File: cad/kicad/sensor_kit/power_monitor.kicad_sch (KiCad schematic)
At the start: 20 parts, among them U2 INA3221

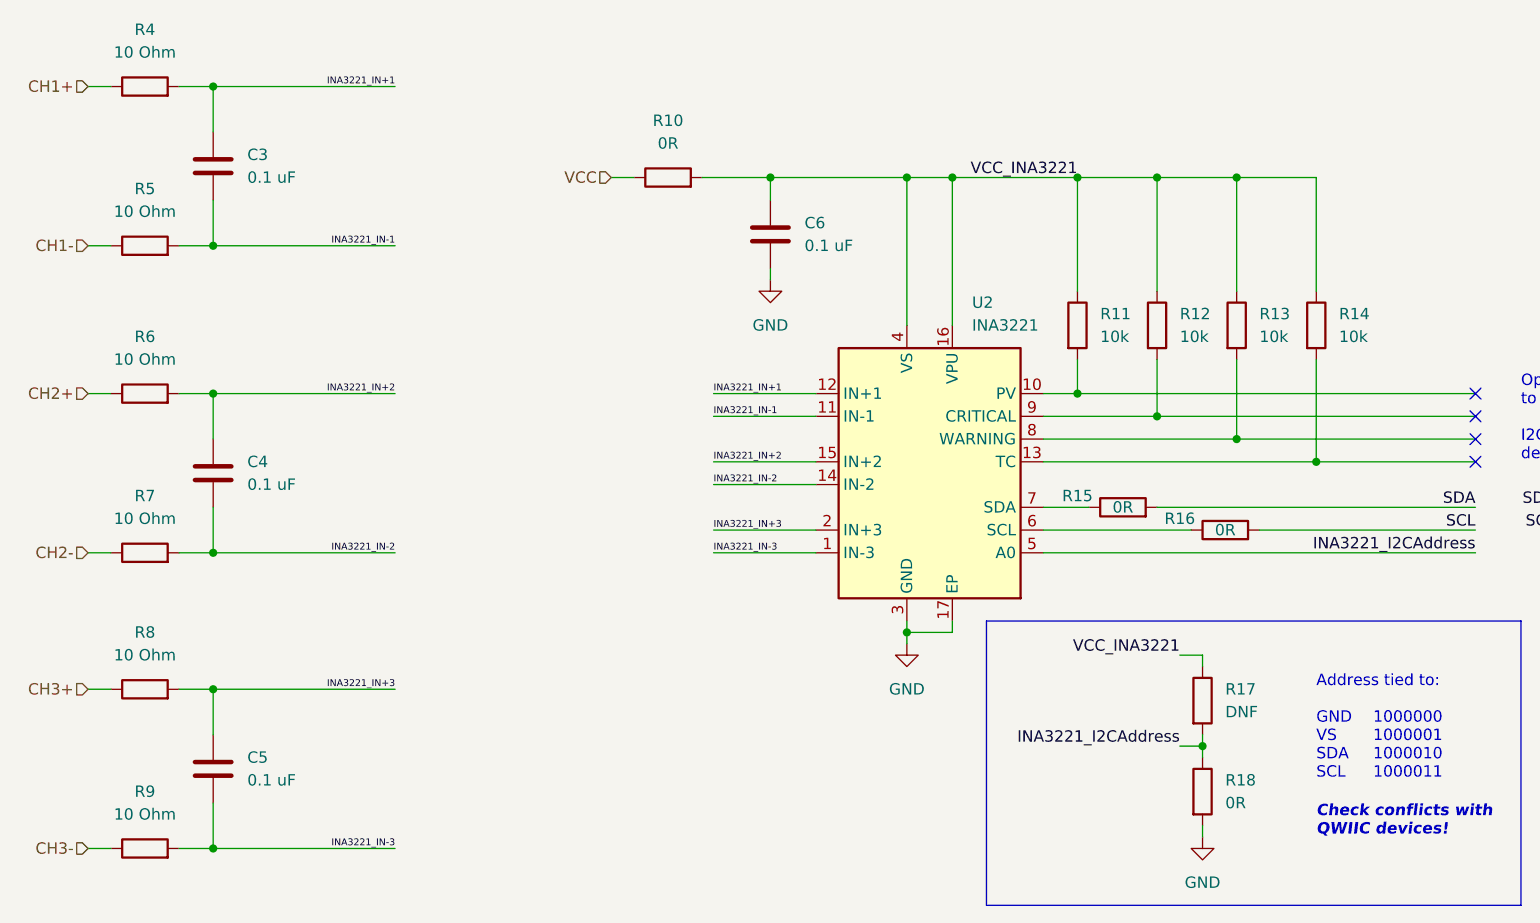
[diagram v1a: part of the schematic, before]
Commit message: adds further sensors to board layout
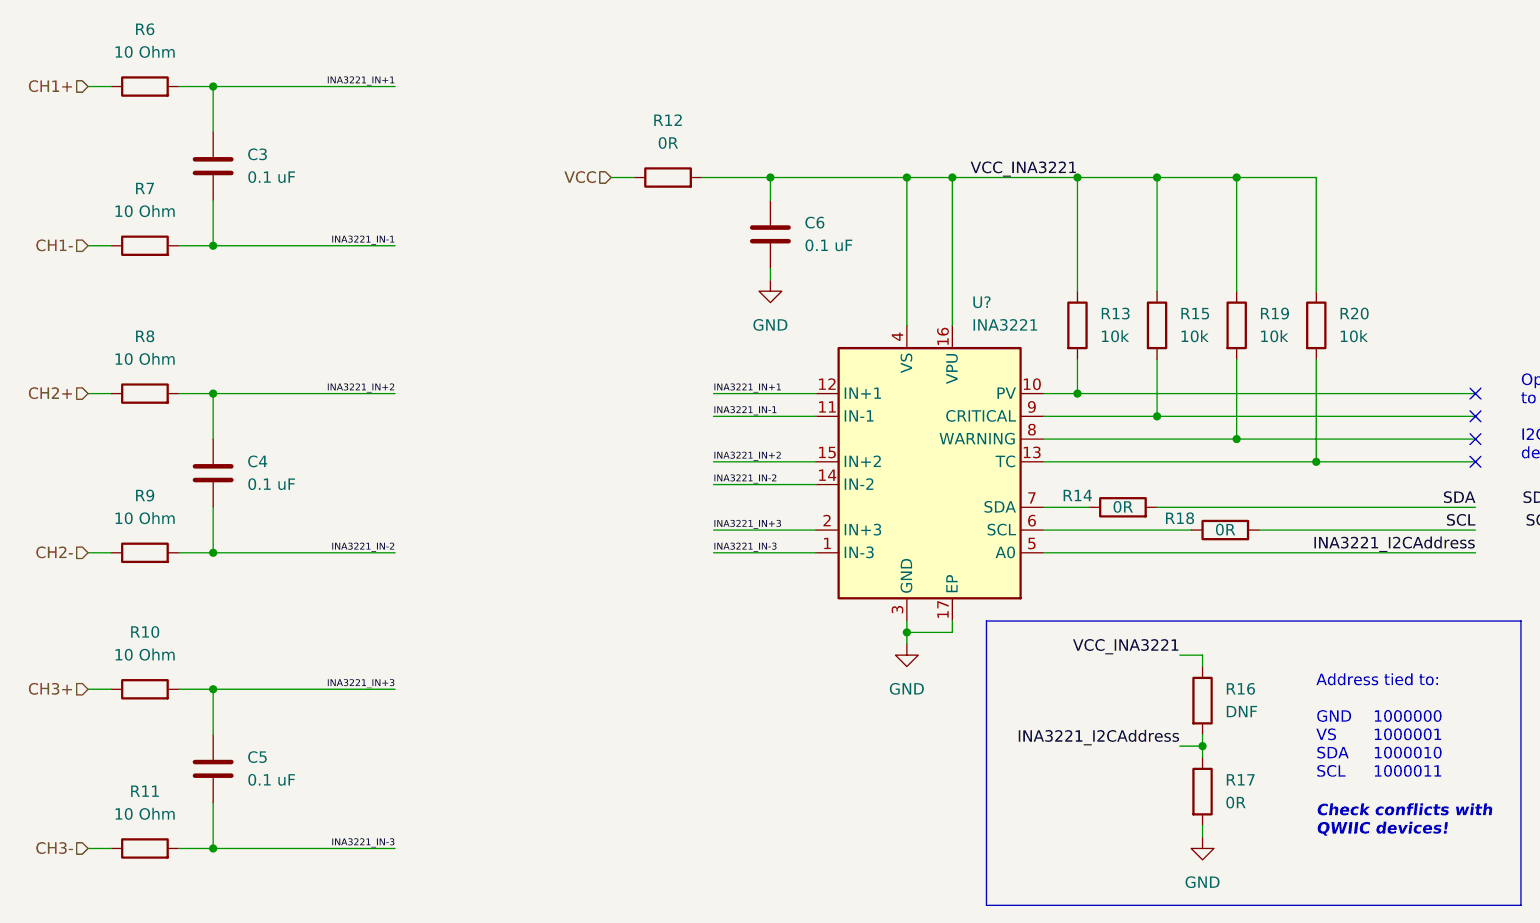
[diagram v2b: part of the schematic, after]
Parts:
- R10: renamed from R8; footprint (none) -> Resistor_SMD:R_1206_3216Metric_Pad1.30x1.75mm_HandSolder
- R11: renamed from R9; footprint (none) -> Resistor_SMD:R_1206_3216Metric_Pad1.30x1.75mm_HandSolder
- R12: renamed from R10; footprint (none) -> Resistor_SMD:R_0805_2012Metric_Pad1.20x1.40mm_HandSolder
- R13: renamed from R11; footprint (none) -> Resistor_SMD:R_0805_2012Metric_Pad1.20x1.40mm_HandSolder
- R14: renamed from R15; footprint (none) -> Resistor_SMD:R_0805_2012Metric_Pad1.20x1.40mm_HandSolder
- R15: renamed from R12; footprint (none) -> Resistor_SMD:R_0805_2012Metric_Pad1.20x1.40mm_HandSolder
- R16: renamed from R17; footprint (none) -> Resistor_SMD:R_0805_2012Metric_Pad1.20x1.40mm_HandSolder
- R17: renamed from R18; footprint (none) -> Resistor_SMD:R_0805_2012Metric_Pad1.20x1.40mm_HandSolder
- R18: renamed from R16; footprint (none) -> Resistor_SMD:R_0805_2012Metric_Pad1.20x1.40mm_HandSolder
- R19: renamed from R13; footprint (none) -> Resistor_SMD:R_0805_2012Metric_Pad1.20x1.40mm_HandSolder
- R20: renamed from R14; footprint (none) -> Resistor_SMD:R_0805_2012Metric_Pad1.20x1.40mm_HandSolder
- R6: renamed from R4; footprint (none) -> Resistor_SMD:R_1206_3216Metric_Pad1.30x1.75mm_HandSolder
- R7: renamed from R5; footprint (none) -> Resistor_SMD:R_1206_3216Metric_Pad1.30x1.75mm_HandSolder
- R8: renamed from R6; footprint (none) -> Resistor_SMD:R_1206_3216Metric_Pad1.30x1.75mm_HandSolder
- R9: renamed from R7; footprint (none) -> Resistor_SMD:R_1206_3216Metric_Pad1.30x1.75mm_HandSolder
- renumbered U2 to U?

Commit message: revises sensor board to remove current source and reduce footprint
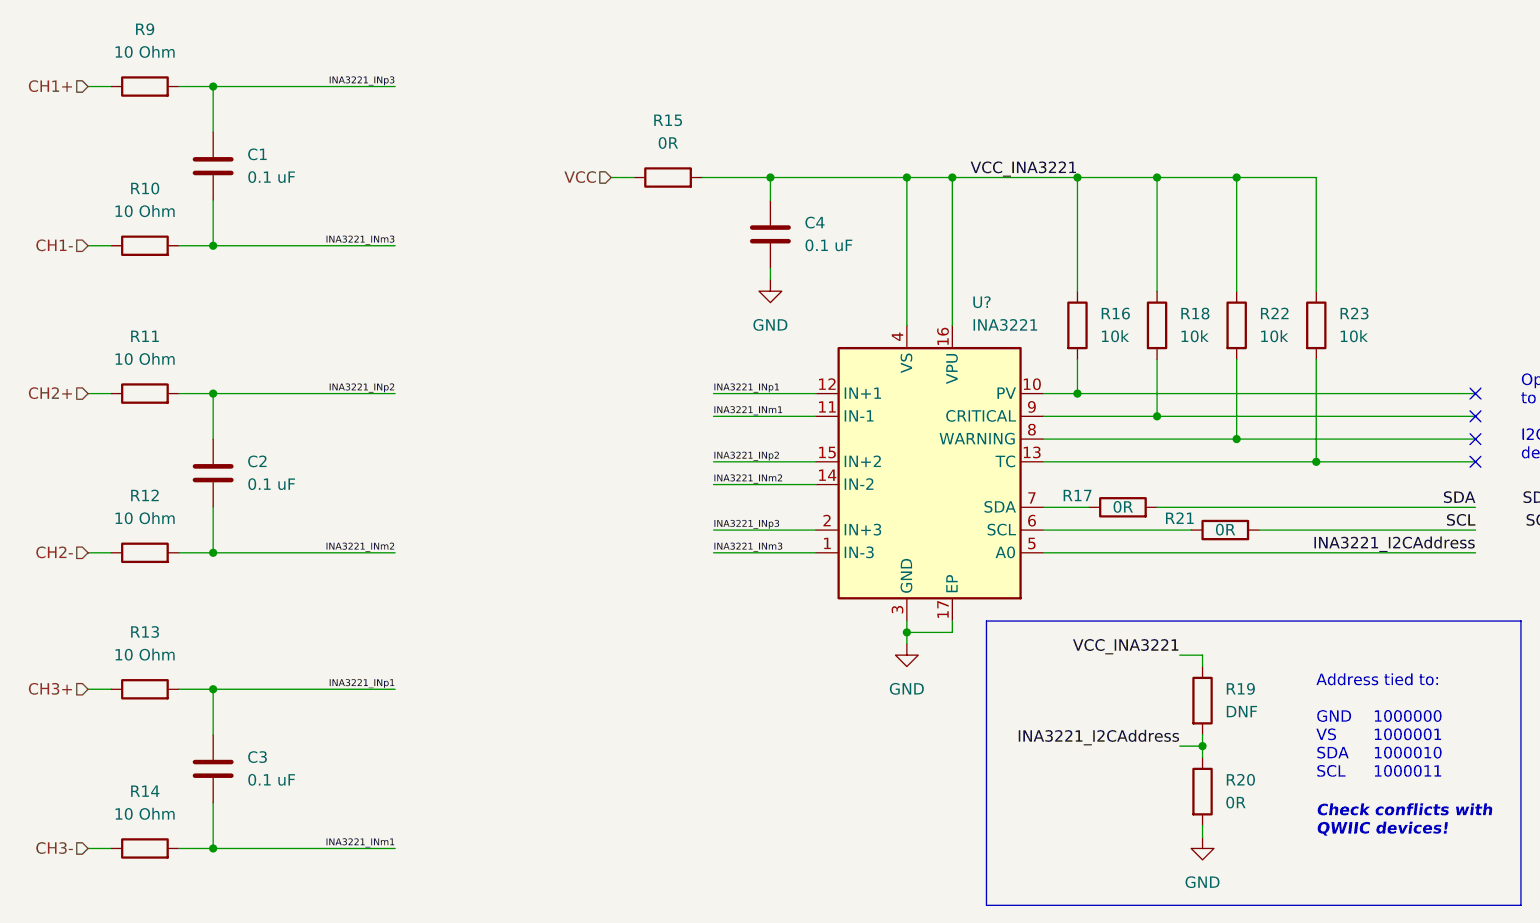
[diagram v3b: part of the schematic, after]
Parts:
- C1: renamed from C3; footprint (none) -> Resistor_SMD:R_0603_1608Metric; Manufacturer (none) -> Kemet; MftrPartNo (none) -> C0603C104M5RACTU
- C2: renamed from C4; footprint (none) -> Resistor_SMD:R_0603_1608Metric; Manufacturer (none) -> Kemet; MftrPartNo (none) -> C0603C104M5RACTU
- C3: renamed from C5; footprint (none) -> Resistor_SMD:R_0603_1608Metric; Manufacturer (none) -> Kemet; MftrPartNo (none) -> C0603C104M5RACTU
- C4: renamed from C6; footprint (none) -> Resistor_SMD:R_0603_1608Metric; Manufacturer (none) -> Kemet; MftrPartNo (none) -> C0603C104M5RACTU
- renumbered R7 to R10, R8 to R11, R9 to R12, R10 to R13, R11 to R14, R12 to R15, R13 to R16, R14 to R17, R15 to R18, R16 to R19, R17 to R20, R18 to R21, R19 to R22, R20 to R23, R6 to R9
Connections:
- net INA3221_IN+1 renamed INA3221_INp3
- net INA3221_INp3: now also U?.2 (IN+3); no longer U?.12 (IN+1)
- net INA3221_IN+2 renamed INA3221_INp2
- net INA3221_IN+3 renamed INA3221_INp1
- net INA3221_INp1: now also U?.12 (IN+1); no longer U?.2 (IN+3)
- net INA3221_IN-1 renamed INA3221_INm3
- net INA3221_INm3: now also U?.1 (IN-3); no longer U?.11 (IN-1)
- net INA3221_IN-2 renamed INA3221_INm2
- net INA3221_IN-3 renamed INA3221_INm1
- net INA3221_INm1: now also U?.11 (IN-1); no longer U?.1 (IN-3)

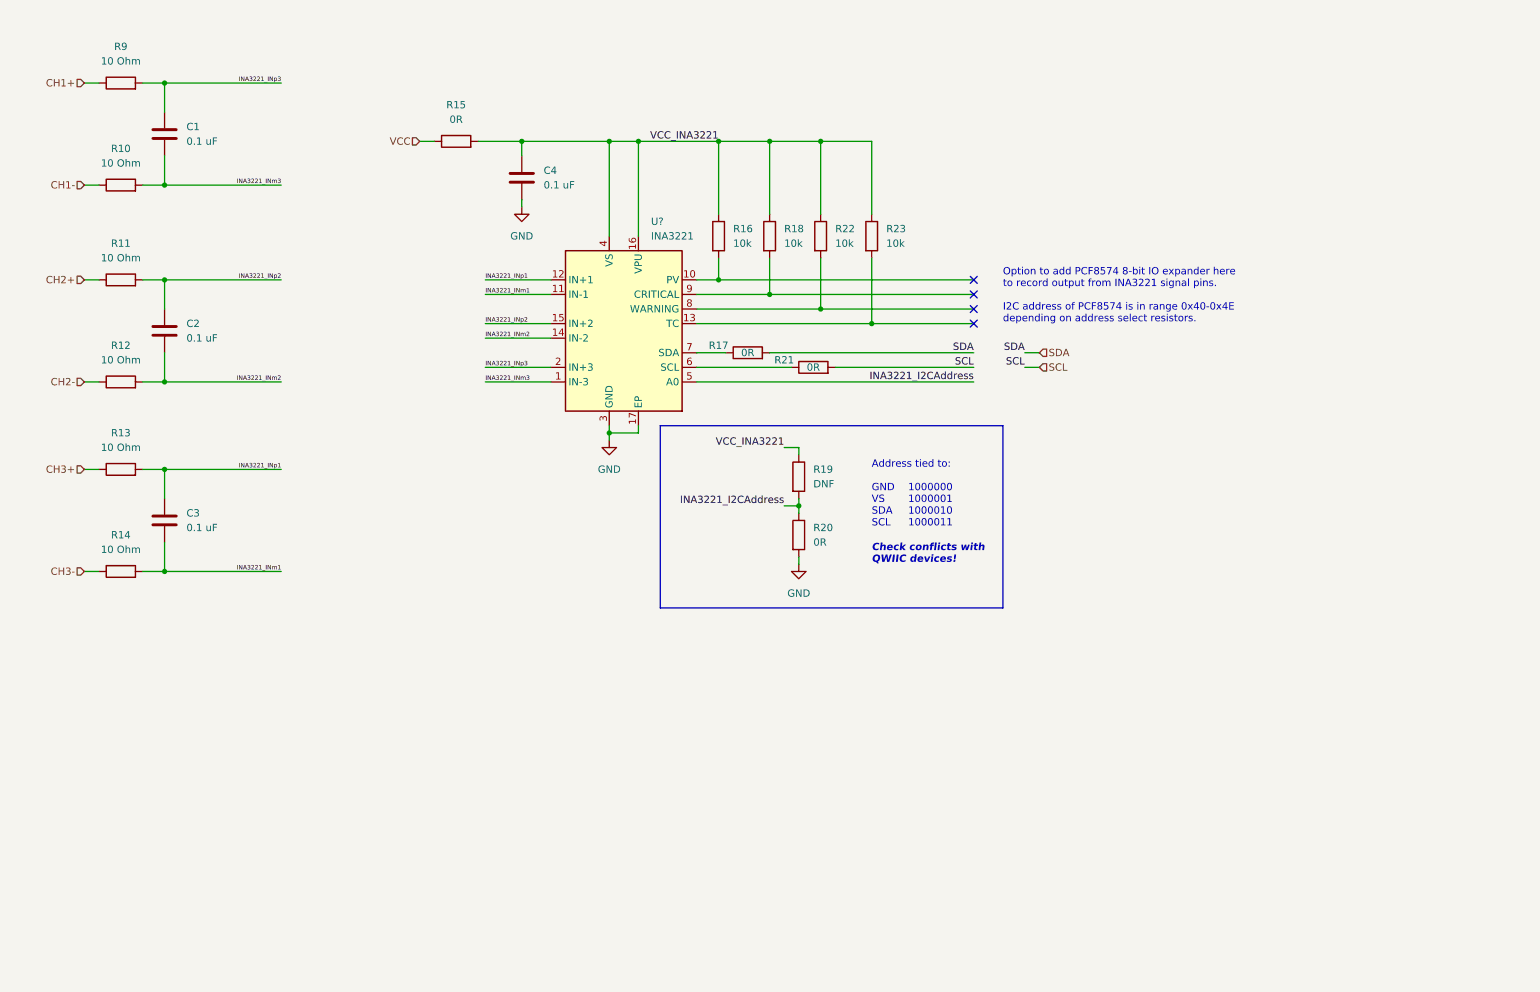
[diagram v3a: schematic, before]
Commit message: fixes MISO/MOSI on RFM96, swaps Dp/Dm on USB and makes pads for THT resistors bigger
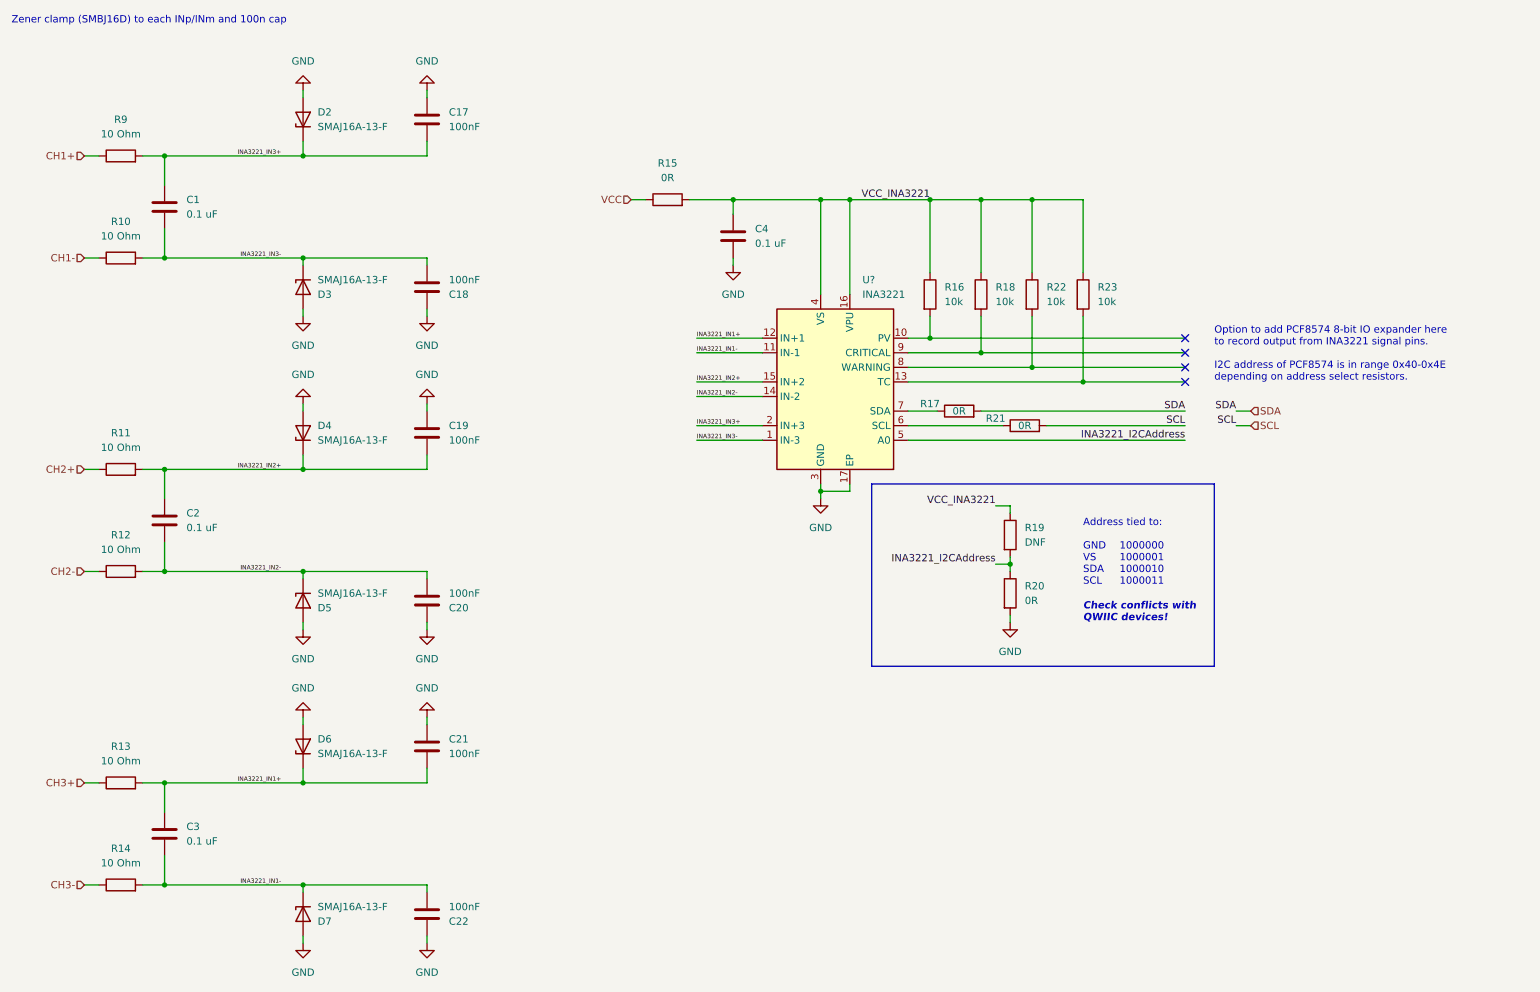
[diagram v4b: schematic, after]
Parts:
- added C17, C18, C19, C20, C21, C22: 100nF, Capacitor_SMD:C_0402_1005Metric, symbol Device:C
- added D2, D3, D4, D5, D6, D7: SMAJ16A-13-F, Diode_SMD:D_SMA, symbol Device:D_Zener
- C1, C2, C3, C4: Placed (none) -> Yes; Supplier (none) -> Farnell; SupplierPartNo (none) -> 2581046
- R10, R11, R12, R13, R14, R9: Manufacturer (none) -> Multicomp Pro; MftrPartNo (none) -> MCWR12X10R0FTL; Placed (none) -> Yes; Supplier (none) -> Farnell; SupplierPartNo (none) -> 2447457
- R15, R17, R20, R21: Manufacturer (none) -> Multicomp Pro; MftrPartNo (none) -> MCWR08X0000FTL; Placed (none) -> Yes; Supplier (none) -> Farnell; SupplierPartNo (none) -> 2747563
- R16, R18, R22, R23: Manufacturer (none) -> Multicomp Pro; MftrPartNo (none) -> MCWR08X1002FTL; Placed (none) -> Yes; Supplier (none) -> Farnell; SupplierPartNo (none) -> 2447553
- R19: Placed (none) -> No
- U?: MftrPartNo (none) -> INA3221; Placed (none) -> Yes; Supplier (none) -> Digi-Key; SupplierPartNo (none) -> 296-INA3221AIRGVRCT-ND
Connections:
- net GND: now also C17.1, C18.1, C19.1, C20.1, C21.1, C22.1, D2.2 (A), D3.2 (A), D4.2 (A), D5.2 (A), D6.2 (A), D7.2 (A)
- net INA3221_INm1 renamed INA3221_IN1-
- net INA3221_IN1-: now also C22.2, D7.1 (K)
- net INA3221_INm2 renamed INA3221_IN2-
- net INA3221_IN2-: now also C20.2, D5.1 (K)
- net INA3221_INm3 renamed INA3221_IN3-
- net INA3221_IN3-: now also C18.2, D3.1 (K)
- net INA3221_INp1 renamed INA3221_IN1+
- net INA3221_IN1+: now also C21.2, D6.1 (K)
- net INA3221_INp2 renamed INA3221_IN2+
- net INA3221_IN2+: now also C19.2, D4.1 (K)
- net INA3221_INp3 renamed INA3221_IN3+
- net INA3221_IN3+: now also C17.2, D2.1 (K)
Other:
- note added: "Zener clamp (SMBJ16D) to each INp/INm and 100n cap"
- moved on the sheet: C1, C2, C3, C4, R10, R11, R12, R13, R14, R15, R16, R17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

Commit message: updates production files from sensor kit materials
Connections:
- net CH1+: now also R13.1; no longer R9.1
- net CH1-: now also R14.1; no longer R10.1
- net CH3+: now also R9.1; no longer R13.1
- net CH3-: now also R10.1; no longer R14.1
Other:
- company: (none) -> Cardiff University & CryoSkills Organising Committee
- title: (none) -> CryoSkills Sensor Kit
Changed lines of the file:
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@@
 (kicad_sch (version 20230121) (generator eeschema)
   (paper "A4")
+  (title_block
+    (title "CryoSkills Sensor Kit")
+    (company "Cardiff University & CryoSkills Organising Committee")
+    (comment 1 "Auth: J. D. Hawkins, L. Craw, M. Prior-Jones, E. Fisher")
+    (comment 2 "Contact: hawkinsj22@cardiff.ac.uk")
+  )
   (junction (at 171.45 55.88) (diameter 0) (color 0 0 0 0)
   )
@@
     (effects (font (size 1.27 1.27)) (justify right))
   )
-  (hierarchical_label "CH1+" (shape input) (at 38.1 48.26 180) (fields_autoplaced)
+  (hierarchical_label "CH1+" (shape input) (at 38.1 157.48 180) (fields_autoplaced)
     (effects (font (size 1.27 1.27)) (justify right))
   )
@@
     (effects (font (size 1.27 1.27)) (justify right))
   )
-  (hierarchical_label "CH1-" (shape input) (at 38.1 66.04 180) (fields_autoplaced)
+  (hierarchical_label "CH1-" (shape input) (at 38.1 175.26 180) (fields_autoplaced)
     (effects (font (size 1.27 1.27)) (justify right))
   )
@@
     (effects (font (size 1.27 1.27)) (justify right))
   )
-  (hierarchical_label "CH3+" (shape input) (at 38.1 157.48 180) (fields_autoplaced)
-    (effects (font (size 1.27 1.27)) (justify right))
-  )
-  (hierarchical_label "CH3-" (shape input) (at 38.1 175.26 180) (fields_autoplaced)
-    (effects (font (size 1.27 1.27)) (justify right))
-  )
+  (hierarchical_label "CH3+" (shape input) (at 38.1 48.26 180) (fields_autoplaced)
+    (effects (font (size 1.27 1.27)) (justify right))
+  )
+  (hierarchical_label "CH3-" (shape input) (at 38.1 66.04 180) (fields_autoplaced)
+    (effects (font (size 1.27 1.27)) (justify right))
+  )
